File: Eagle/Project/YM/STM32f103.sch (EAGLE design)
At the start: 78 parts, among them IC1 YM3812, IC10 YM3812, IC11 YM3014B, IC12 LM358N, IC13 BA033CC0T, IC14 74ALS04N, IC15 6N136, IC2 YM3014B, IC3 LM358N, IC4 YM3812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

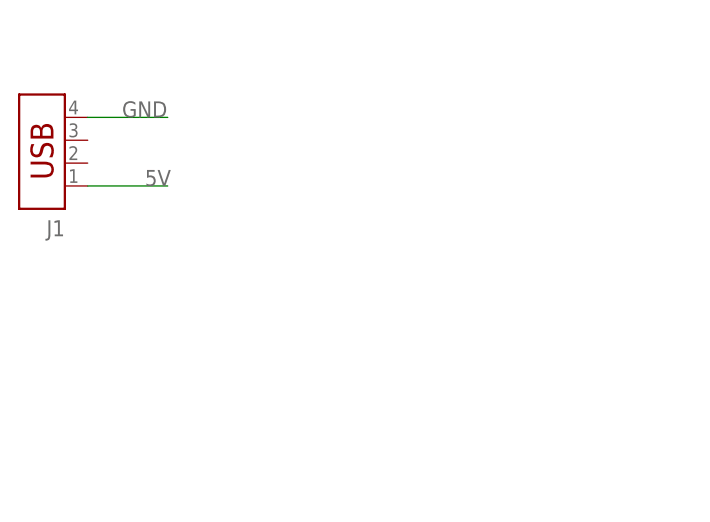
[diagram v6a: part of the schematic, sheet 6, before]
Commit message: V4.0 ON/OFF Button/LED
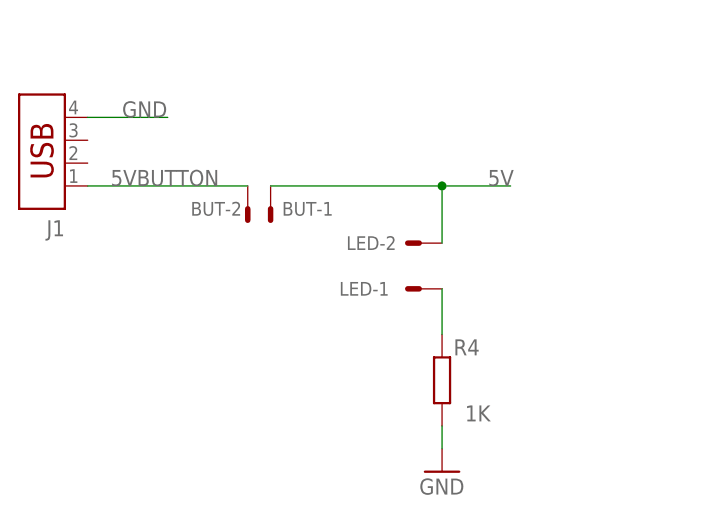
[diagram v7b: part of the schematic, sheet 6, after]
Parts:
- added BUT, LED: 22-27-2021-02, con-molex:22-27-2021-02
- added R4: 1K, +HU-Lib:1K
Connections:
- new net 5VBUTTON: BUT-2.S, J1.1
- new net N$13: LED-1.S, R4.1
- net 5V: now also BUT-1.S, LED-2.S; no longer J1.1
- net GND: now also R4.2
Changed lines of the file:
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@@
 <part name="SV3" library="2514-6002UB" deviceset="2514-6002UB" device=""/>
 <part name="SV4" library="con-lsta" library_urn="urn:adsk.eagle:library:161" deviceset="FE13-1" device="" package3d_urn="urn:adsk.eagle:package:8213/1"/>
+<part name="BUT" library="con-molex" library_urn="urn:adsk.eagle:library:165" deviceset="22-?-02" device="27-2021" package3d_urn="urn:adsk.eagle:package:8078645/1"/>
+<part name="LED" library="con-molex" library_urn="urn:adsk.eagle:library:165" deviceset="22-?-02" device="27-2021" package3d_urn="urn:adsk.eagle:package:8078645/1"/>
+<part name="R4" library="+HU-Lib" deviceset="1K" device=""/>
+<part name="GND38" library="supply1" library_urn="urn:adsk.eagle:library:371" deviceset="GND" device=""/>
 </parts>
 <sheets>
@@
 <attribute name="VALUE" x="53.34" y="106.68" size="1.778" layer="96" rot="R180"/>
 </instance>
+<instance part="BUT" gate="-1" x="76.2" y="91.44" smashed="yes" rot="R270">
+<attribute name="NAME" x="77.47" y="90.678" size="1.524" layer="95"/>
+</instance>
+<instance part="BUT" gate="-2" x="73.66" y="91.44" smashed="yes" rot="R270">
+<attribute name="NAME" x="67.31" y="90.678" size="1.524" layer="95"/>
+</instance>
+<instance part="LED" gate="-1" x="92.71" y="82.55" smashed="yes" rot="R180">
+<attribute name="NAME" x="83.82" y="81.788" size="1.524" layer="95"/>
+</instance>
+<instance part="LED" gate="-2" x="92.71" y="87.63" smashed="yes" rot="R180">
+<attribute name="NAME" x="90.17" y="88.392" size="1.524" layer="95" rot="R180"/>
+</instance>
+<instance part="R4" gate="G$1" x="95.25" y="72.39" smashed="yes" rot="R270">
+<attribute name="NAME" x="96.52" y="75.1586" size="1.778" layer="95"/>
+<attribute name="VALUE" x="97.79" y="67.818" size="1.778" layer="96"/>
+</instance>
+<instance part="GND38" gate="1" x="95.25" y="62.23" smashed="yes">
+<attribute name="VALUE" x="92.71" y="59.69" size="1.778" layer="96"/>
+</instance>
 </instances>
 <busses>
@@
 </segment>
 <segment>
-<pinref part="J1" gate="G$1" pin="1"/>
-<wire x1="55.88" y1="93.98" x2="64.77" y2="93.98" width="0.1524" layer="91"/>
-<label x="62.23" y="93.98" size="1.778" layer="95"/>
+<pinref part="BUT" gate="-1" pin="S"/>
+<wire x1="76.2" y1="93.98" x2="95.25" y2="93.98" width="0.1524" layer="91"/>
+<label x="100.33" y="93.98" size="1.778" layer="95"/>
+<pinref part="LED" gate="-2" pin="S"/>
+<wire x1="95.25" y1="93.98" x2="95.25" y2="87.63" width="0.1524" layer="91"/>
+<wire x1="95.25" y1="93.98" x2="102.87" y2="93.98" width="0.1524" layer="91"/>
+<junction x="95.25" y="93.98"/>
 </segment>
 </net>
@@
 <label x="59.69" y="101.6" size="1.778" layer="95"/>
 </segment>
+<segment>
+<pinref part="R4" gate="G$1" pin="2"/>
+<wire x1="95.25" y1="67.31" x2="95.25" y2="64.77" width="0.1524" layer="91"/>
+<pinref part="GND38" gate="1" pin="GND"/>
+</segment>
 </net>
 <net name="3.3V" class="0">
@@
 </segment>
 </net>
+<net name="5VBUTTON" class="0">
+<segment>
+<pinref part="J1" gate="G$1" pin="1"/>
+<wire x1="55.88" y1="93.98" x2="73.66" y2="93.98" width="0.1524" layer="91"/>
+<label x="58.42" y="93.98" size="1.778" layer="95"/>
+<pinref part="BUT" gate="-2" pin="S"/>
+</segment>
+</net>
+<net name="N$13" class="0">
+<segment>
+<pinref part="LED" gate="-1" pin="S"/>
+<wire x1="95.25" y1="82.55" x2="95.25" y2="77.47" width="0.1524" layer="91"/>
+<pinref part="R4" gate="G$1" pin="1"/>
+</segment>
+</net>
